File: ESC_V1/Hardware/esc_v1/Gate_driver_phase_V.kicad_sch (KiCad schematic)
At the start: 9 parts, among them U7 UCC27282DR

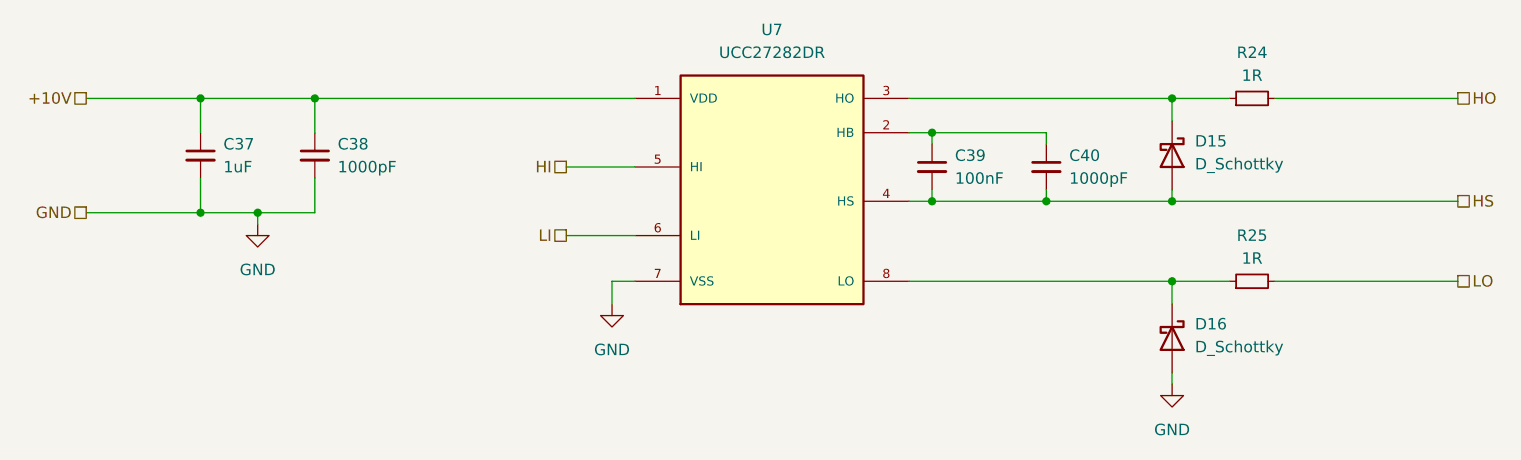
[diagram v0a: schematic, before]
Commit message: Components roughly placed in layout
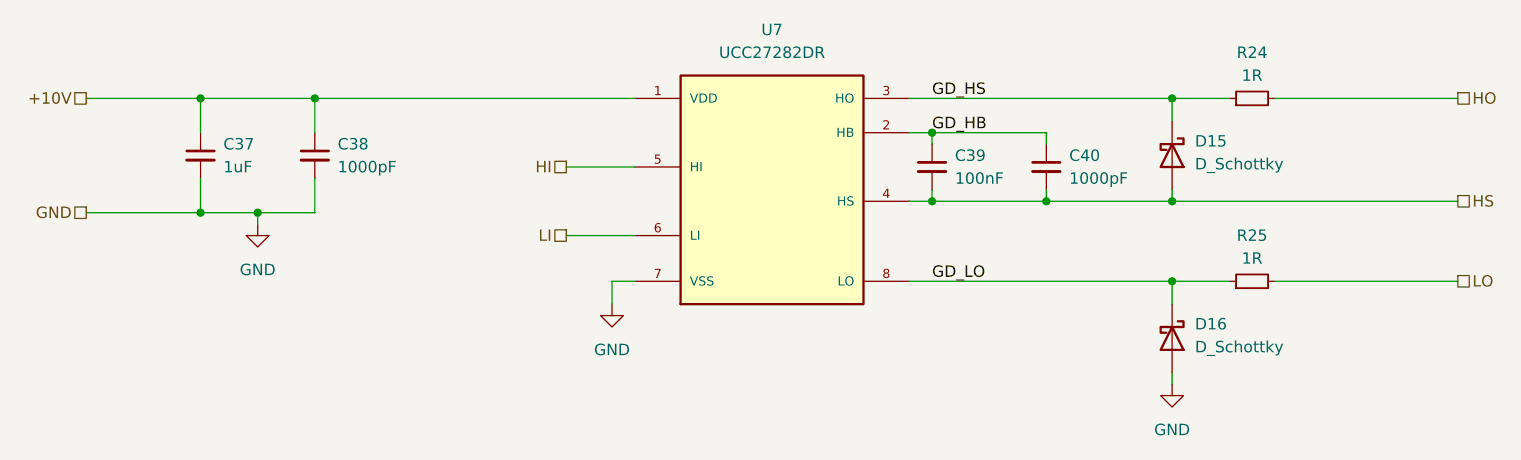
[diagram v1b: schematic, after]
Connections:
- net GD_HB: now reaches C39.1, C40.1, U7.2 (HB)
- net GD_HS: now reaches D15.1 (K), R24.1, U7.3 (HO)
- net GD_LO: now reaches D16.1 (K), R25.1, U7.8 (LO)
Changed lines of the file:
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@@
     (stroke (width 0) (type default) (color 0 0 0 0))
+  )
+  (label "GD_HB" (at 157.48 92.71 0)
+    (effects (font (size 1.27 1.27)) (justify left bottom))
+  )
+  (label "GD_LO" (at 157.48 109.22 0)
+    (effects (font (size 1.27 1.27)) (justify left bottom))
+  )
+  (label "GD_HS" (at 157.48 88.9 0)
+    (effects (font (size 1.27 1.27)) (justify left bottom))
   )
   (hierarchical_label "HI" (shape passive) (at 116.84 96.52 180)
